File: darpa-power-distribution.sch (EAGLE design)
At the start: 78 parts, among them J1 61300211121, Q1 IRFR5305, Q2 IRFR5305, Q3 IRFR5305, X1 MKDSN1,5/2-5,08, X10 MKDSN1,5/2-5,08, X2 MKDSN1,5/2-5,08, X3 MKDSN1,5/2-5,08, X4 MKDSN1,5/2-5,08, X5 MKDSN1,5/2-5,08, X6 MKDSN1,5/2-5,08, X7 MKDSN1,5/2-5,08, X8 MKDSN1,5/2-5,08, X9 MKDSN1,5/2-5,08

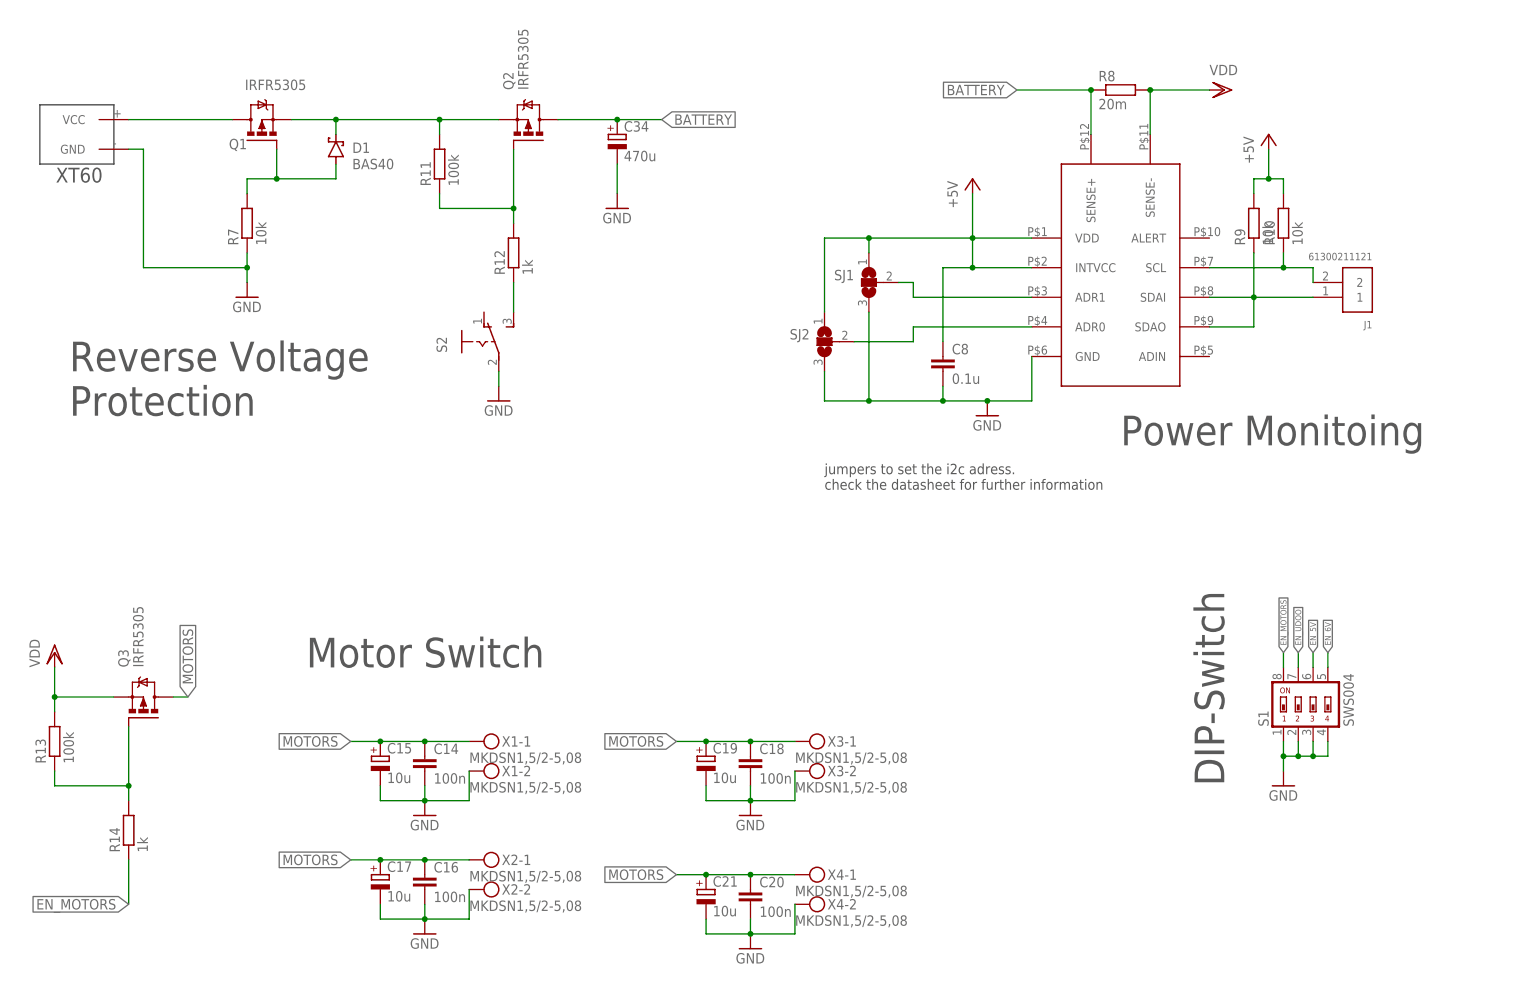
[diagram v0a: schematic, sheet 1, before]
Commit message: placing improved. routing proceeded
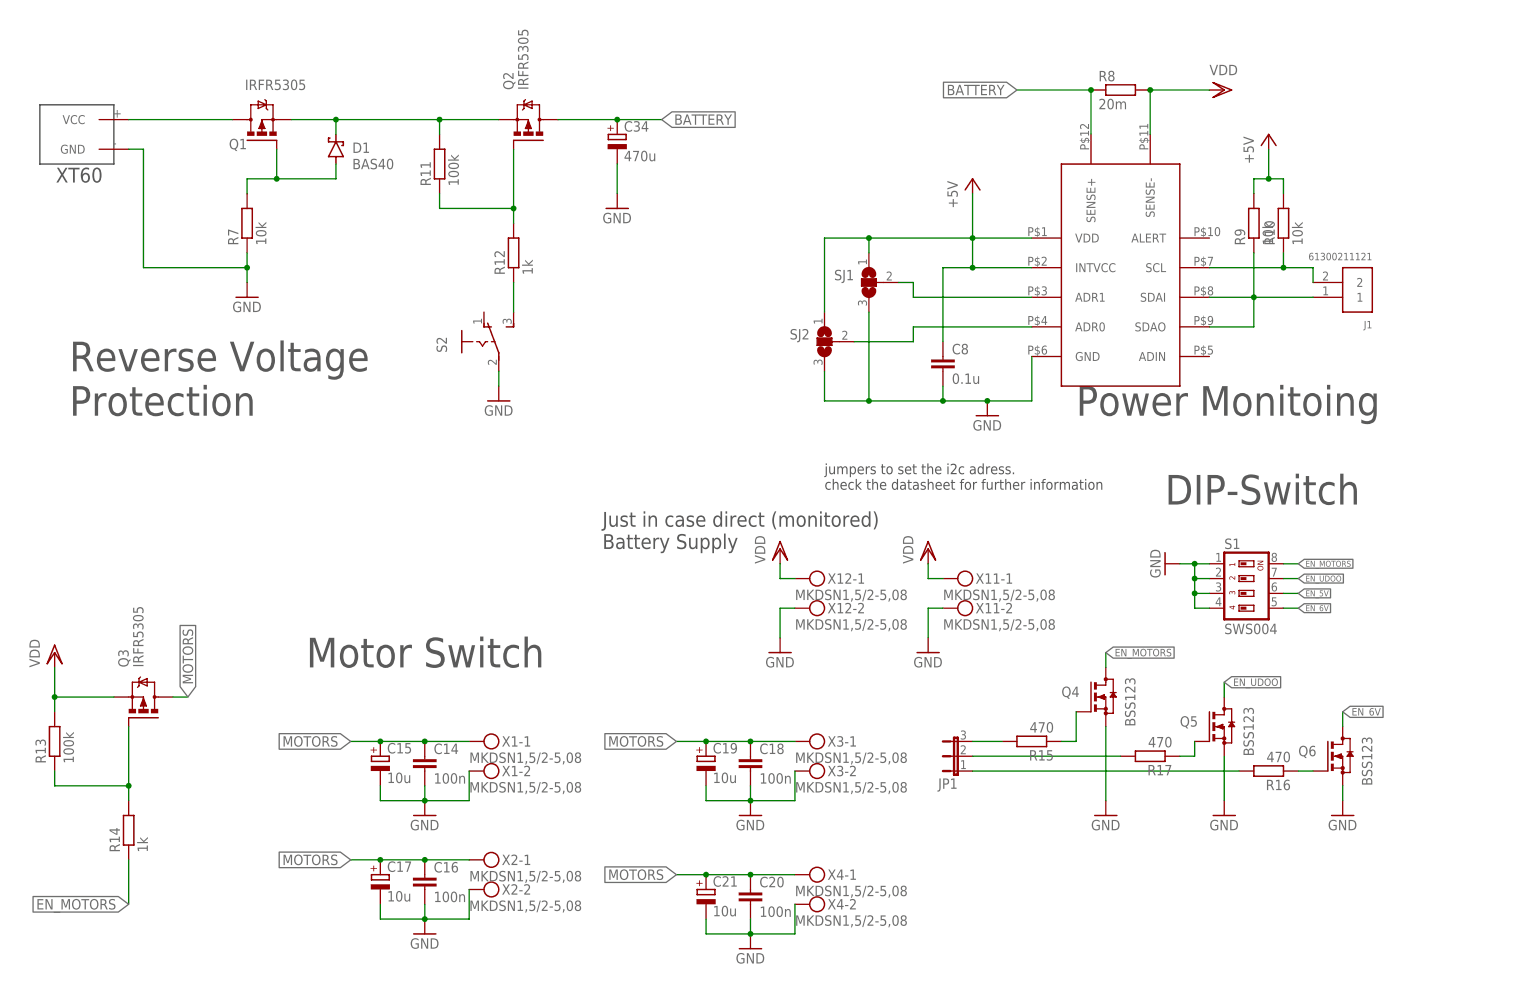
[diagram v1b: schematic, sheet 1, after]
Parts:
- added JP1: (no value), jumper:JP2E
- added Q4, Q5, Q6: BSS123, transistor-small-signal:BSS123
- added R15, R16: 470, rcl:R-EU_R0805
- added X11, X12: MKDSN1,5/2-5,08, con-phoenix-508:MKDSN1,5/2-5,08
- R17: value 10k -> 470
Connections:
- new net N$16: Q5.G, R17.1
- new net N$19: Q4.G, R15.1
- new net N$21: JP1.3, R15.2
- new net N$22: JP1.1, R16.2
- new net N$23: Q6.G, R16.1
- new net N$8: JP1.2, R17.2
- net EN_6V: now also Q6.D
- net EN_MOTORS: now also Q4.D
- net EN_UDOO: now also Q5.D; no longer R17.2
- net GND: now also Q4.S, Q5.S, Q6.S, X11-2.KL, X12-2.KL
- net VDD: now also X11-1.KL, X12-1.KL; no longer R17.1
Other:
- note added: "Just in case direct (monitored) Battery Supply"
- moved on the sheet: S1

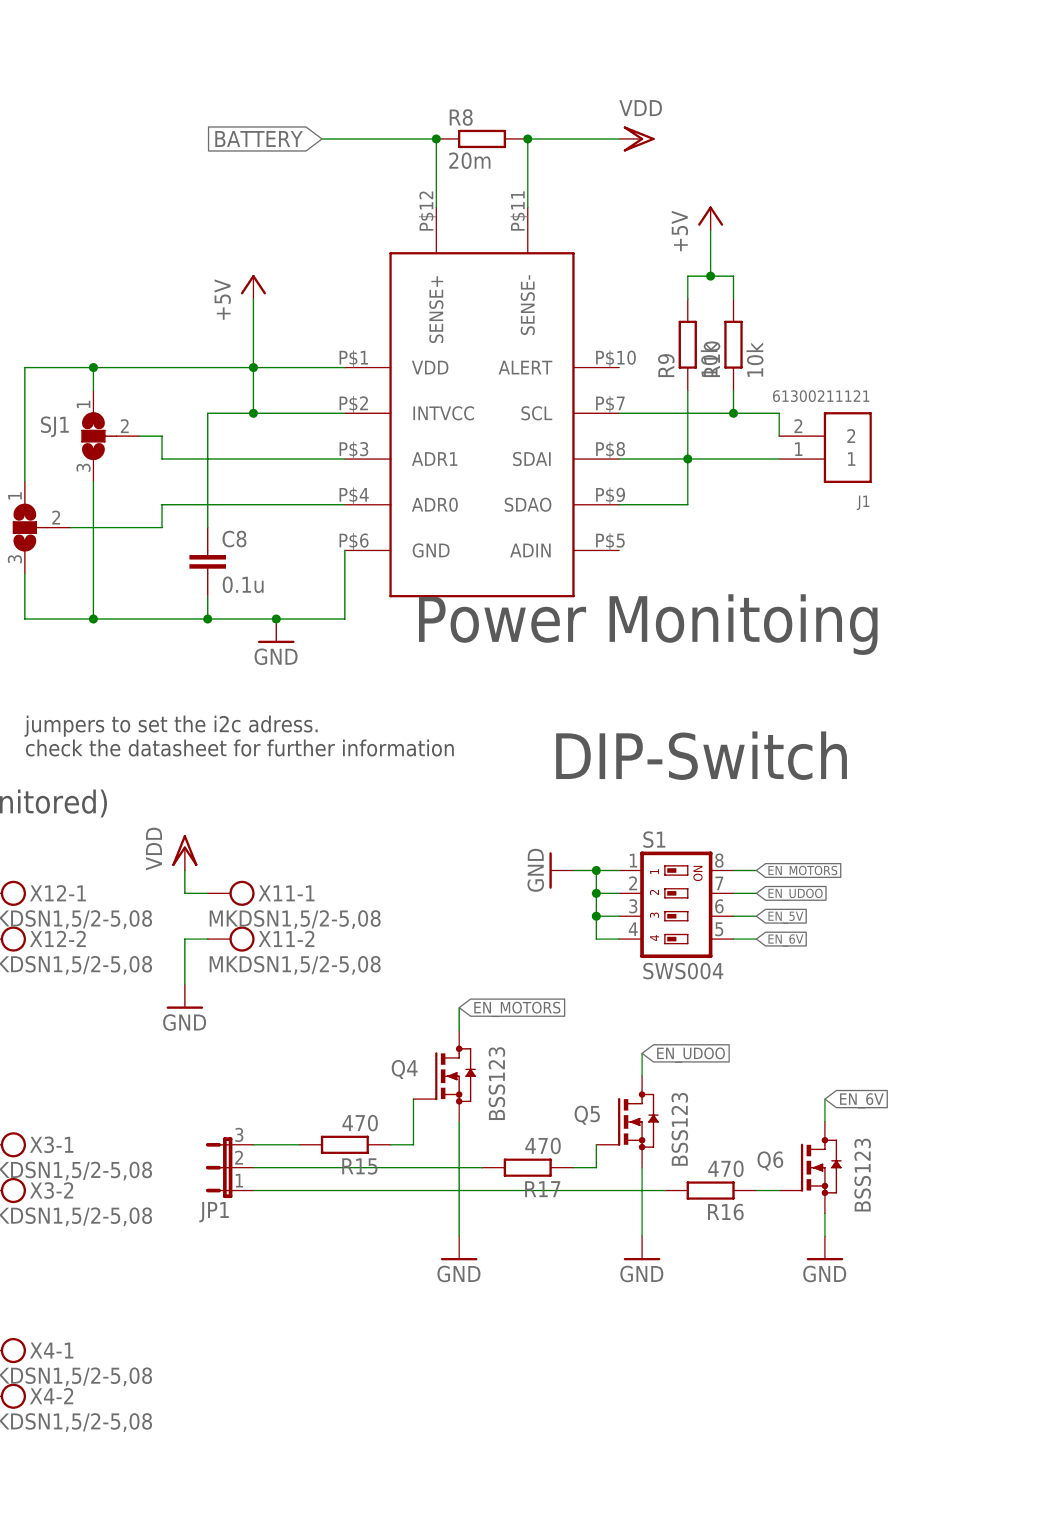
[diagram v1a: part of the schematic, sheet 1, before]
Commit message: routing completed; Errors fixed; added LEDs and BOM; TODO: DRC, second cheack and approval
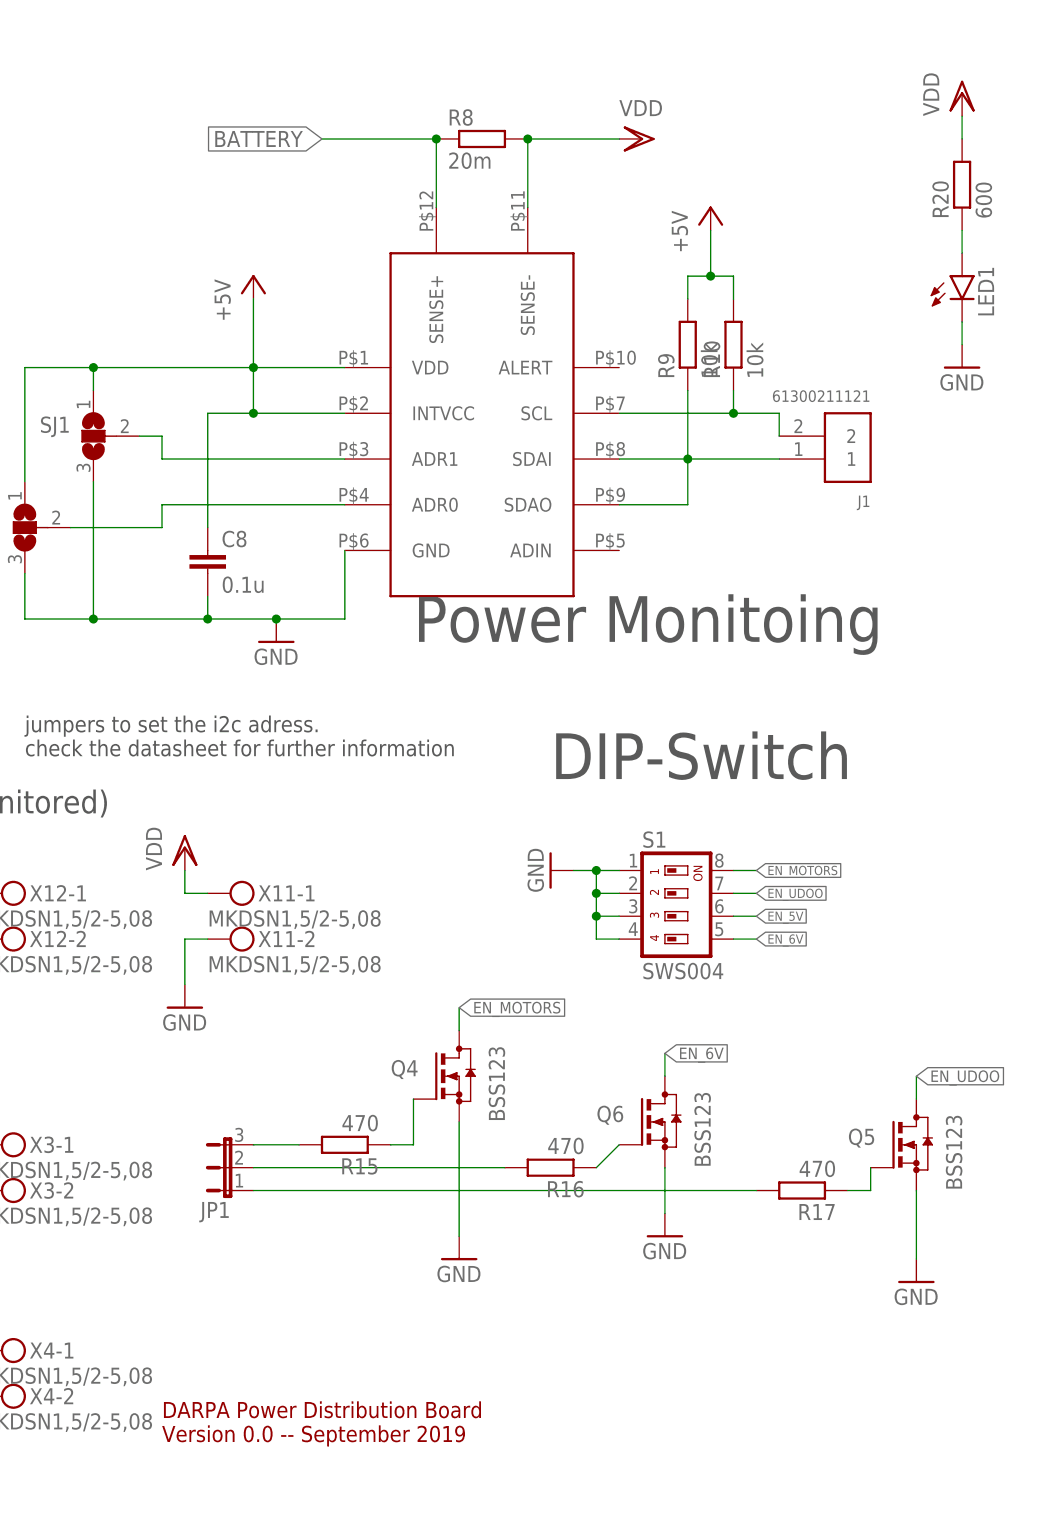
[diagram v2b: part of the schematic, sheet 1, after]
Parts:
- added LED1, LED2, LED3, LED4: (no value), led:LEDSML0805
- added R20, R23: 600, rcl:R-EU_R0805
- added R21, R22: 200, rcl:R-EU_R0805
- C14, C16, C18, C20, C22, C24, C26, C28, C30, C32: device rcl:C-EUC0805 -> rcl:C-EUC0805K
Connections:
- new net N$27: LED1.A, R20.1
- new net N$28: LED2.A, R21.1
- new net N$29: LED3.A, R22.1
- new net N$30: LED4.A, R23.1
- net +5V: now also R21.2
- net 12V_UDOO: now also R23.2
- net 6V_SERVO: now also R22.2
- net GND: now also LED1.C, LED2.C, LED3.C, LED4.C
- net N$22: now also JP1.2; no longer JP1.1
- net N$8: now also JP1.1; no longer JP1.2
- net VDD: now also R20.2
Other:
- note added: "DARPA Power Distribution Board Version 0.0 -- September 2019"
- moved on the sheet: Q5, Q6, R16, R17

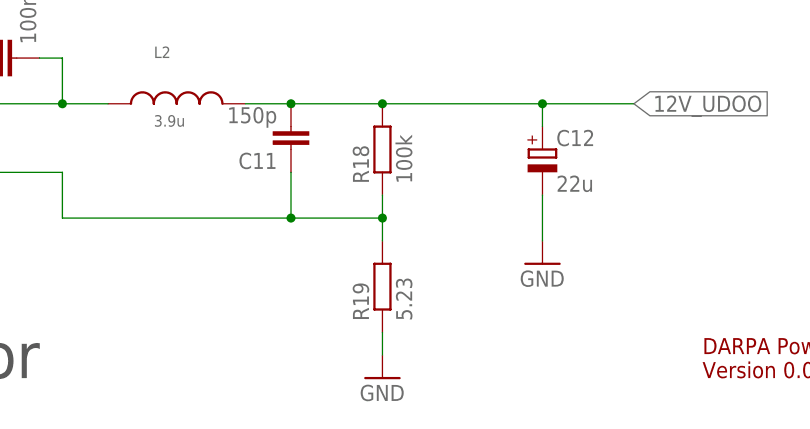
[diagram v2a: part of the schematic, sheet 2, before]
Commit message: corrected typo in resistor value
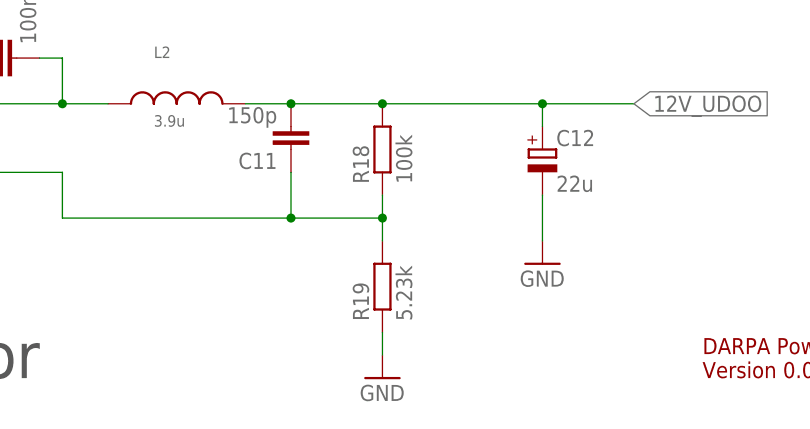
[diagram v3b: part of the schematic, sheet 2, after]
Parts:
- R19: value 5.23 -> 5.23k
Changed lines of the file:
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@@
 <part name="VDD5" library="supply1" library_urn="urn:adsk.eagle:library:371" deviceset="VDD" device=""/>
 <part name="R18" library="rcl" library_urn="urn:adsk.eagle:library:334" deviceset="R-EU_" device="R0805" package3d_urn="urn:adsk.eagle:package:23553/2" value="100k"/>
-<part name="R19" library="rcl" library_urn="urn:adsk.eagle:library:334" deviceset="R-EU_" device="R0805" package3d_urn="urn:adsk.eagle:package:23553/2" value="5.23"/>
+<part name="R19" library="rcl" library_urn="urn:adsk.eagle:library:334" deviceset="R-EU_" device="R0805" package3d_urn="urn:adsk.eagle:package:23553/2" value="5.23k"/>
 <part name="L2" library="Wurth_Elektronik_Passive_rev19e" library_urn="urn:adsk.eagle:library:7584915" deviceset="WE-CHSA_1011" device="" package3d_urn="urn:adsk.eagle:package:7587046/5" technology="_7843330330" value="3.9u"/>
 <part name="GND11" library="supply1" library_urn="urn:adsk.eagle:library:371" deviceset="GND" device=""/>

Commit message: placing improved, DRC done, labels aligned
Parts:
- renumbered J1 to I2C, JP1 to JP_ENABLE, LED1 to POWER, LED2 to 5V, LED3 to 6V, R23 to 12V, S1 to ENABLE, S2 to ON/OFF, U$1 to 5V_REG, U$2 to 6V_REG, U$5 to 12V_REG
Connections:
- net N$21 renamed JP_MOTORS
- net N$22 renamed JP_6V
- net N$8 renamed JP_12V
